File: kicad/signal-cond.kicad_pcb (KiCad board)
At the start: 2 copper layers, 14.5 x 28 mm, 12 parts

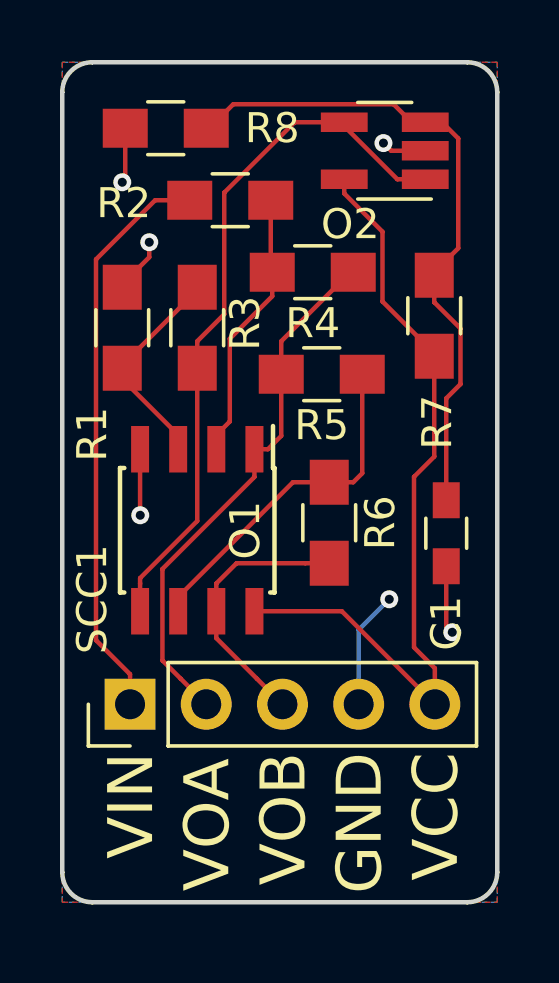
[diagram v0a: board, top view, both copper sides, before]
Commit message: improved routing
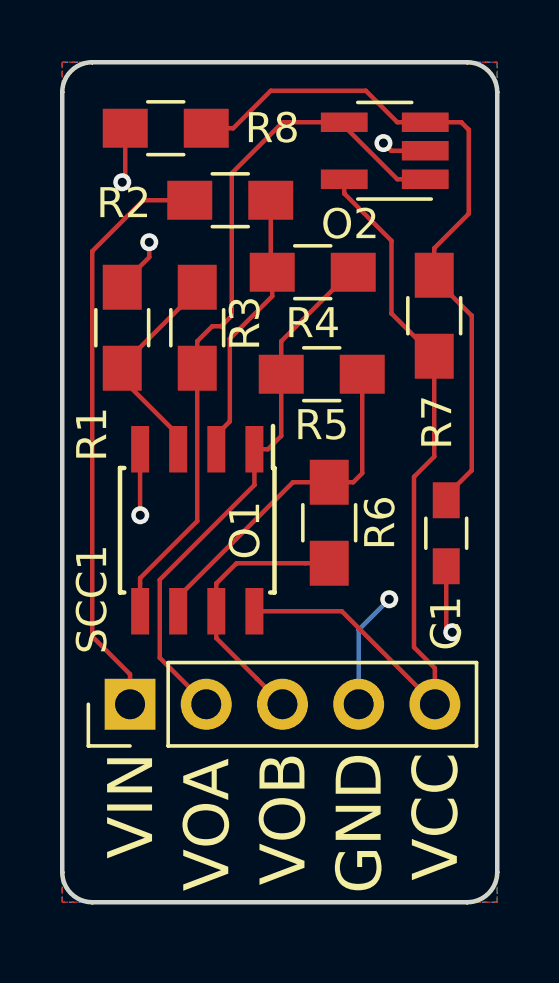
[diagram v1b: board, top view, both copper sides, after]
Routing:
- net Net-(C1-Pad1): track 22.2 -> 24.7 mm
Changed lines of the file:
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@@
     (links 26)
     (no_connects 0)
-    (area 144.975 97.625 164.066667 130.335714)
+    (area 144.924999 97.625 164.066667 130.335714)
     (thickness 1.6)
     (drawings 14)
-    (tracks 107)
+    (tracks 112)
     (zones 0)
     (modules 12)
@@
     (effects (font (size 1.5 1.5) (thickness 0.3)) (justify right))
   )
-  (segment (start 157.8 113.1) (end 157.8 109.705002) (width 0.15) (layer F.Cu) (net 1))
-  (segment (start 157.8 109.705002) (end 158.275001 109.230001) (width 0.15) (layer F.Cu) (net 1))
-  (segment (start 158.275001 109.230001) (end 158.275001 107.375001) (width 0.15) (layer F.Cu) (net 1))
-  (segment (start 158.275001 107.375001) (end 157.4 106.5) (width 0.15) (layer F.Cu) (net 1))
-  (segment (start 157.4 106.5) (end 157.4 105.6) (width 0.15) (layer F.Cu) (net 1))
+  (segment (start 151.95 99.45) (end 155.12 99.45) (width 0.15) (layer F.Cu) (net 1))
+  (segment (start 155.12 99.45) (end 156.17 100.5) (width 0.15) (layer F.Cu) (net 1))
+  (segment (start 156.17 100.5) (end 157.1 100.5) (width 0.15) (layer F.Cu) (net 1))
+  (segment (start 149.8 100.7) (end 150.7 100.7) (width 0.15) (layer F.Cu) (net 1))
+  (segment (start 150.7 100.7) (end 151.95 99.45) (width 0.15) (layer F.Cu) (net 1))
+  (segment (start 158.55 100.75) (end 158.3 100.5) (width 0.15) (layer F.Cu) (net 1))
+  (segment (start 158.3 100.5) (end 157.1 100.5) (width 0.15) (layer F.Cu) (net 1))
+  (segment (start 158.55 103.55) (end 158.55 100.75) (width 0.15) (layer F.Cu) (net 1))
+  (segment (start 157.4 105.6) (end 157.4 104.7) (width 0.15) (layer F.Cu) (net 1))
+  (segment (start 157.4 104.7) (end 158.55 103.55) (width 0.15) (layer F.Cu) (net 1))
+  (segment (start 157.8 113.1) (end 157.8 112.95) (width 0.15) (layer F.Cu) (net 1))
+  (segment (start 157.8 112.95) (end 158.65 112.1) (width 0.15) (layer F.Cu) (net 1))
+  (segment (start 158.65 112.1) (end 158.65 106.95) (width 0.15) (layer F.Cu) (net 1))
+  (segment (start 158.65 106.95) (end 157.4 105.7) (width 0.15) (layer F.Cu) (net 1))
+  (segment (start 157.4 105.7) (end 157.4 105.6) (width 0.15) (layer F.Cu) (net 1))
   (segment (start 157.1 100.5) (end 157.660002 100.5) (width 0.15) (layer F.Cu) (net 1))
-  (segment (start 157.660002 100.5) (end 158.2 101.039998) (width 0.15) (layer F.Cu) (net 1))
-  (segment (start 158.2 101.039998) (end 158.2 104.7) (width 0.15) (layer F.Cu) (net 1))
-  (segment (start 158.2 104.7) (end 157.4 105.5) (width 0.15) (layer F.Cu) (net 1))
   (segment (start 157.4 105.5) (end 157.4 105.6) (width 0.15) (layer F.Cu) (net 1))
   (segment (start 157.1 100.5) (end 156.645 100.5) (width 0.15) (layer F.Cu) (net 1))
-  (segment (start 150.7 99.9) (end 149.9 100.7) (width 0.15) (layer F.Cu) (net 1))
-  (segment (start 156.645 100.5) (end 156.045 99.9) (width 0.15) (layer F.Cu) (net 1))
-  (segment (start 156.045 99.9) (end 150.7 99.9) (width 0.15) (layer F.Cu) (net 1))
   (segment (start 149.9 100.7) (end 149.8 100.7) (width 0.15) (layer F.Cu) (net 1))
   (segment (start 157.8 115.3) (end 157.8 117.3) (width 0.15) (layer F.Cu) (net 2))
@@
   (segment (start 147.9 105) (end 147.9 104.5) (width 0.15) (layer F.Cu) (net 2))
   (via (at 147.9 104.5) (size 0.6) (drill 0.3) (layers F.Cu B.Cu) (net 2))
-  (segment (start 151.405 111.4) (end 151.405 112.325) (width 0.15) (layer F.Cu) (net 3))
-  (segment (start 148.950001 119.050001) (end 149.8 119.9) (width 0.15) (layer F.Cu) (net 3))
-  (segment (start 151.405 112.325) (end 148.339999 115.390001) (width 0.15) (layer F.Cu) (net 3))
-  (segment (start 148.339999 115.390001) (end 148.339999 118.439999) (width 0.15) (layer F.Cu) (net 3))
-  (segment (start 148.339999 118.439999) (end 148.950001 119.050001) (width 0.15) (layer F.Cu) (net 3))
+  (segment (start 148.25 115.75) (end 148.25 118.35) (width 0.15) (layer F.Cu) (net 3))
+  (segment (start 148.25 118.35) (end 149.8 119.9) (width 0.15) (layer F.Cu) (net 3))
+  (segment (start 151.405 112.595) (end 148.25 115.75) (width 0.15) (layer F.Cu) (net 3))
+  (segment (start 151.405 111.4) (end 151.405 112.595) (width 0.15) (layer F.Cu) (net 3))
   (segment (start 152.3 108.9) (end 152.3 107.8) (width 0.15) (layer F.Cu) (net 3))
   (segment (start 154.6 105.5) (end 154.7 105.5) (width 0.15) (layer F.Cu) (net 3))
@@
   (segment (start 147.5 108.7) (end 147.5 108.1) (width 0.1) (layer F.Cu) (net 5))
   (segment (start 147.5 108.8) (end 147.5 108.7) (width 0.1) (layer F.Cu) (net 5))
-  (segment (start 150.4 102.844998) (end 150.4 106.9) (width 0.15) (layer F.Cu) (net 6))
-  (segment (start 154.4 100.5) (end 152.744998 100.5) (width 0.15) (layer F.Cu) (net 6))
-  (segment (start 152.744998 100.5) (end 150.4 102.844998) (width 0.15) (layer F.Cu) (net 6))
-  (segment (start 150.4 106.9) (end 149.5 107.8) (width 0.15) (layer F.Cu) (net 6))
-  (segment (start 149.5 107.8) (end 149.5 108.7) (width 0.15) (layer F.Cu) (net 6))
+  (segment (start 149.5 108.7) (end 149.5 107.8) (width 0.15) (layer F.Cu) (net 6))
+  (segment (start 149.5 107.8) (end 150 107.3) (width 0.15) (layer F.Cu) (net 6))
+  (segment (start 152.35 100.5) (end 154.4 100.5) (width 0.15) (layer F.Cu) (net 6))
+  (segment (start 150 107.3) (end 150.3 107.3) (width 0.15) (layer F.Cu) (net 6))
+  (segment (start 150.3 107.3) (end 150.65 106.95) (width 0.15) (layer F.Cu) (net 6))
+  (segment (start 150.65 106.95) (end 150.65 102.2) (width 0.15) (layer F.Cu) (net 6))
+  (segment (start 150.65 102.2) (end 152.35 100.5) (width 0.15) (layer F.Cu) (net 6))
   (segment (start 157.1 102.4) (end 156.17 102.4) (width 0.15) (layer F.Cu) (net 6))
   (segment (start 156.17 102.4) (end 154.4 100.63) (width 0.15) (layer F.Cu) (net 6))
@@
   (segment (start 150.135 117.695) (end 151.490001 119.050001) (width 0.15) (layer F.Cu) (net 8))
   (segment (start 150.135 116.8) (end 150.135 116.325) (width 0.1) (layer F.Cu) (net 8))
+  (segment (start 155.975 106.875) (end 157.4 108.3) (width 0.15) (layer F.Cu) (net 9))
+  (segment (start 155.975 104.45) (end 155.975 106.875) (width 0.15) (layer F.Cu) (net 9))
+  (segment (start 154.4 102.4) (end 154.4 102.875) (width 0.15) (layer F.Cu) (net 9))
+  (segment (start 154.4 102.875) (end 155.975 104.45) (width 0.15) (layer F.Cu) (net 9))
   (segment (start 157.4 108.3) (end 157.4 108.2) (width 0.15) (layer F.Cu) (net 9))
-  (segment (start 157.4 108.2) (end 155.675001 106.475001) (width 0.15) (layer F.Cu) (net 9))
-  (segment (start 155.675001 106.475001) (end 155.675001 104.150001) (width 0.15) (layer F.Cu) (net 9))
-  (segment (start 155.675001 104.150001) (end 154.4 102.875) (width 0.15) (layer F.Cu) (net 9))
-  (segment (start 154.4 102.875) (end 154.4 102.4) (width 0.15) (layer F.Cu) (net 9))
   (segment (start 157.4 108.3) (end 157.4 111.644998) (width 0.15) (layer F.Cu) (net 9))
   (segment (start 157.4 111.644998) (end 156.724999 112.319999) (width 0.15) (layer F.Cu) (net 9))
@@
   (segment (start 154.32 116.8) (end 157.42 119.9) (width 0.15) (layer F.Cu) (net 9))
   (segment (start 151.405 116.8) (end 151.405 117.275) (width 0.1) (layer F.Cu) (net 9))
-  (segment (start 149.25 103.1) (end 148.094998 103.1) (width 0.15) (layer F.Cu) (net 10))
-  (segment (start 148.094998 103.1) (end 146.124999 105.069999) (width 0.15) (layer F.Cu) (net 10))
-  (segment (start 146.124999 105.069999) (end 146.124999 117.764999) (width 0.15) (layer F.Cu) (net 10))
-  (segment (start 146.124999 117.764999) (end 147.26 118.9) (width 0.15) (layer F.Cu) (net 10))
+  (segment (start 149.25 103.1) (end 147.7 103.1) (width 0.15) (layer F.Cu) (net 10))
+  (segment (start 147.7 103.1) (end 146 104.8) (width 0.15) (layer F.Cu) (net 10))
+  (segment (start 146 104.8) (end 146 117.64) (width 0.15) (layer F.Cu) (net 10))
   (segment (start 147.26 118.9) (end 147.26 119.9) (width 0.15) (layer F.Cu) (net 10))
+  (segment (start 146 117.64) (end 147.26 118.9) (width 0.15) (layer F.Cu) (net 10))
   (zone (net 2) (net_name GND) (layer F.Cu) (hatch edge 0.508)
     (connect_pads (clearance 0.508))
